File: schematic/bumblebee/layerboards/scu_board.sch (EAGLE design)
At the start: 5 parts

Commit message: RC платок аппарата
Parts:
- added P1, P2: B6B-EH-A, con-jst-eh:B6B-EH-A
- added P3: B7B-EH-A, con-jst-eh:B7B-EH-A
- added P4: B5B-EH-A, con-jst-eh:B5B-EH-A
- added P5, P6: B4B-EH-A, con-jst-eh:B4B-EH-A
- added P7: B3B-EH-A, con-jst-eh:B3B-EH-A
- added R1: (no value), ngspice-simulation:R
- added U$6: MCP2551, MCP2551:MCP2551
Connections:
- removed net LIGHT0: U$5.A0
- removed net LIGHT1: U$5.A1
- removed net LIGHT2: U$5.A2
- removed net LIGHT3: U$5.A3
- removed net LIGHT4: U$4.A0
- removed net LIGHT5: U$4.A1
- removed net LIGHT6: U$4.A2
- removed net LIGHT7: U$4.A3
- new net 5V_PCU: U$6.VDD
- new net N$10: P1.3, U$5.A2
- new net N$11: P1.2, U$5.A3
- new net N$12: P2.5, U$4.A0
- new net N$13: P2.4, U$4.A1
- new net N$14: P2.3, U$4.A2
- new net N$15: P2.2, U$4.A3
- new net N$16: U$1.PA11, U$6.RXD
- new net N$17: P3.5, U$1.PC1
- new net N$18: P3.6, U$1.PB1
- new net N$19: U$1.PA12, U$6.TXD
- new net N$20: R1.1, U$6.RS
- new net N$21: P4.2, P6.4
- new net N$22: P5.1, U$1.SW-DAT
- new net N$23: P4.3, P6.3, U$6.CANH
- new net N$24: P5.2, U$1.SW-CLK
- new net N$25: P4.4, P6.2, U$6.CANL
- new net N$26: P5.3, P7.3
- new net N$27: P5.4, P7.2
- new net N$8: P1.5, U$5.A0
- new net N$9: P1.4, U$5.A1
- net 5V_SCU: now also P1.6, P2.6, P3.7, P4.1
- net GND: now also P1.1, P2.1, P3.1, P4.5, P6.1, R1.2, U$6.VSS
- net MAG_CLOCK: now also P3.3
- net MAG_CS: now also P3.2
- net MAG_DATA: now also P3.4

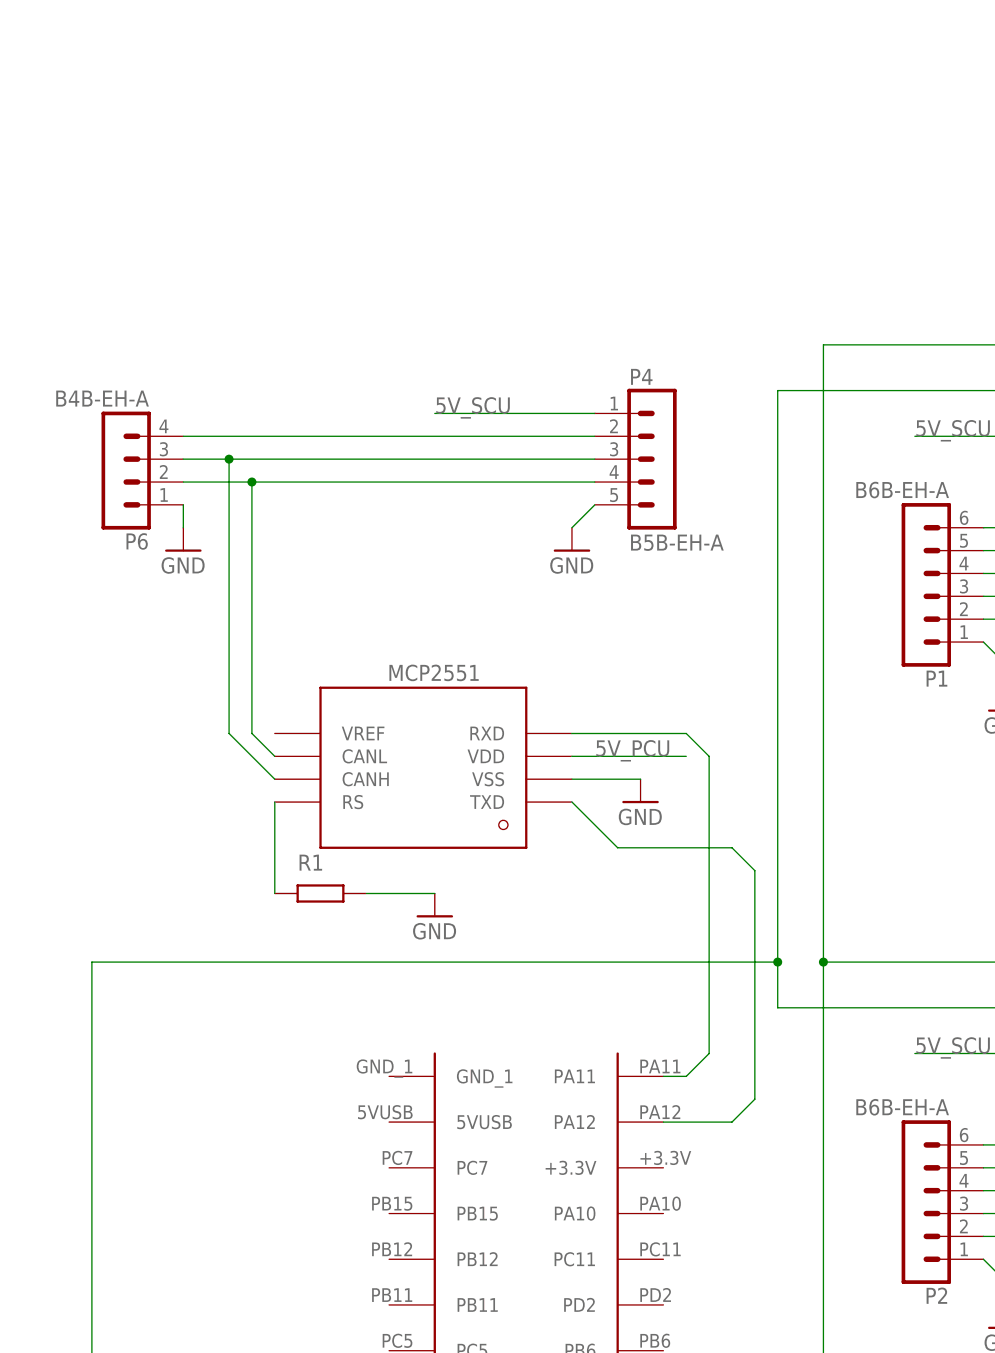
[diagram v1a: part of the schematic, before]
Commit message: Добавил либу SparkFun Идёт работа над CCU и SCU
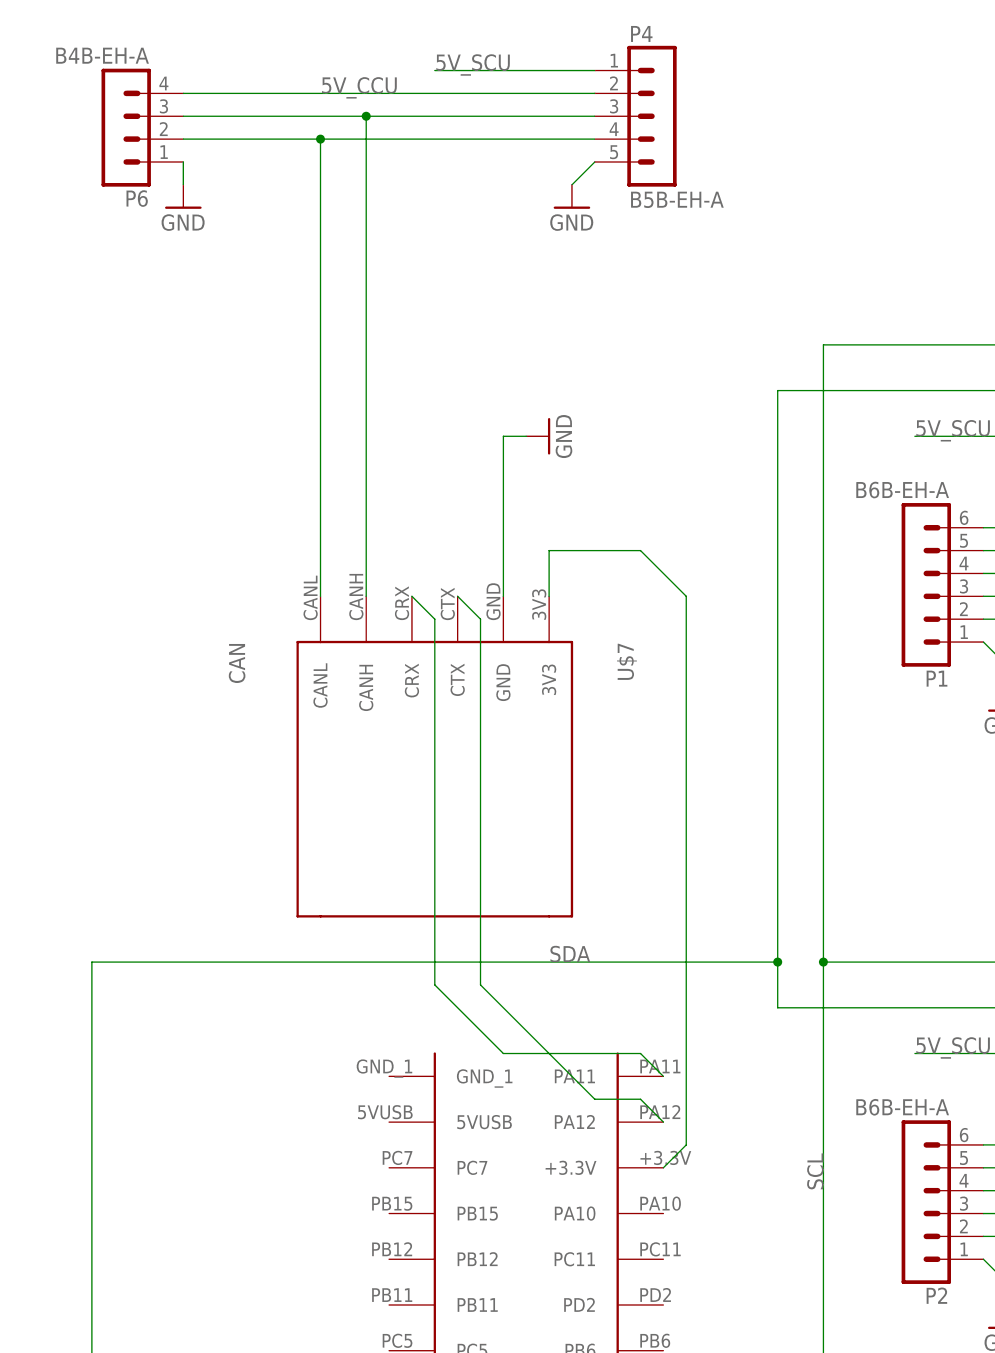
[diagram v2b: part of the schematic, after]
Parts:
- removed R1: (no value), ngspice-simulation:R
- removed U$6: MCP2551, MCP2551:MCP2551
- added U$7: CAN, bluepill:CAN
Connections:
- net N$21 renamed 5V_CCU
- net N$6 renamed SCL
- net N$7 renamed SDA
- removed net 5V_PCU: U$6.VDD
- removed net N$19: U$1.PA12, U$6.TXD
- removed net N$20: R1.1, U$6.RS
- new net N$6: U$1.PA11, U$7.CRX
- new net N$7: U$1.PA12, U$7.CTX
- net GND: now also U$7.GND; no longer R1.2, U$6.VSS
- net N$16: now also U$1.+3.3V, U$7.3V3; no longer U$1.PA11, U$6.RXD
- net N$23: now also U$7.CANH; no longer U$6.CANH
- net N$25: now also U$7.CANL; no longer U$6.CANL
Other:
- moved on the sheet: P4, P6

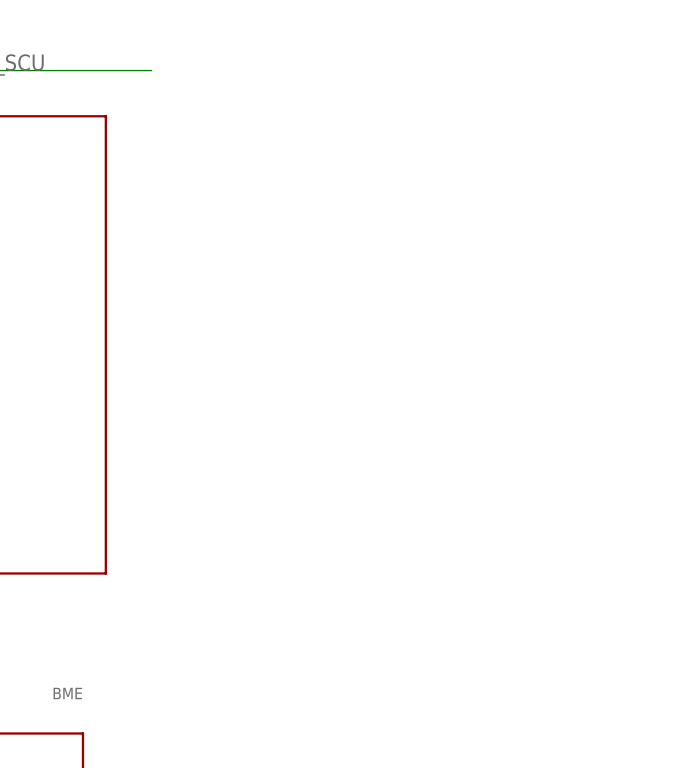
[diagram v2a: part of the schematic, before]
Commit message: Ведётся работа по платам. Готовы SCU и CCU
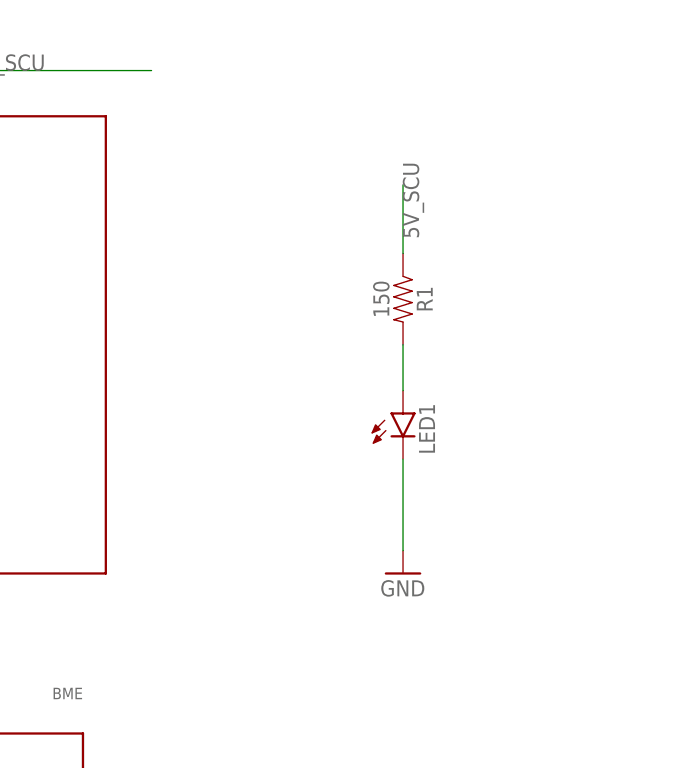
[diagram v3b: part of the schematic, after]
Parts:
- added LED1: (no value), led:LED5MM
- added R1: 150, SparkFun-Resistors:RESISTORAXIAL-0.3
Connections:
- new net N$19: LED1.A, R1.2
- net 5V_SCU: now also R1.1
- net GND: now also LED1.C

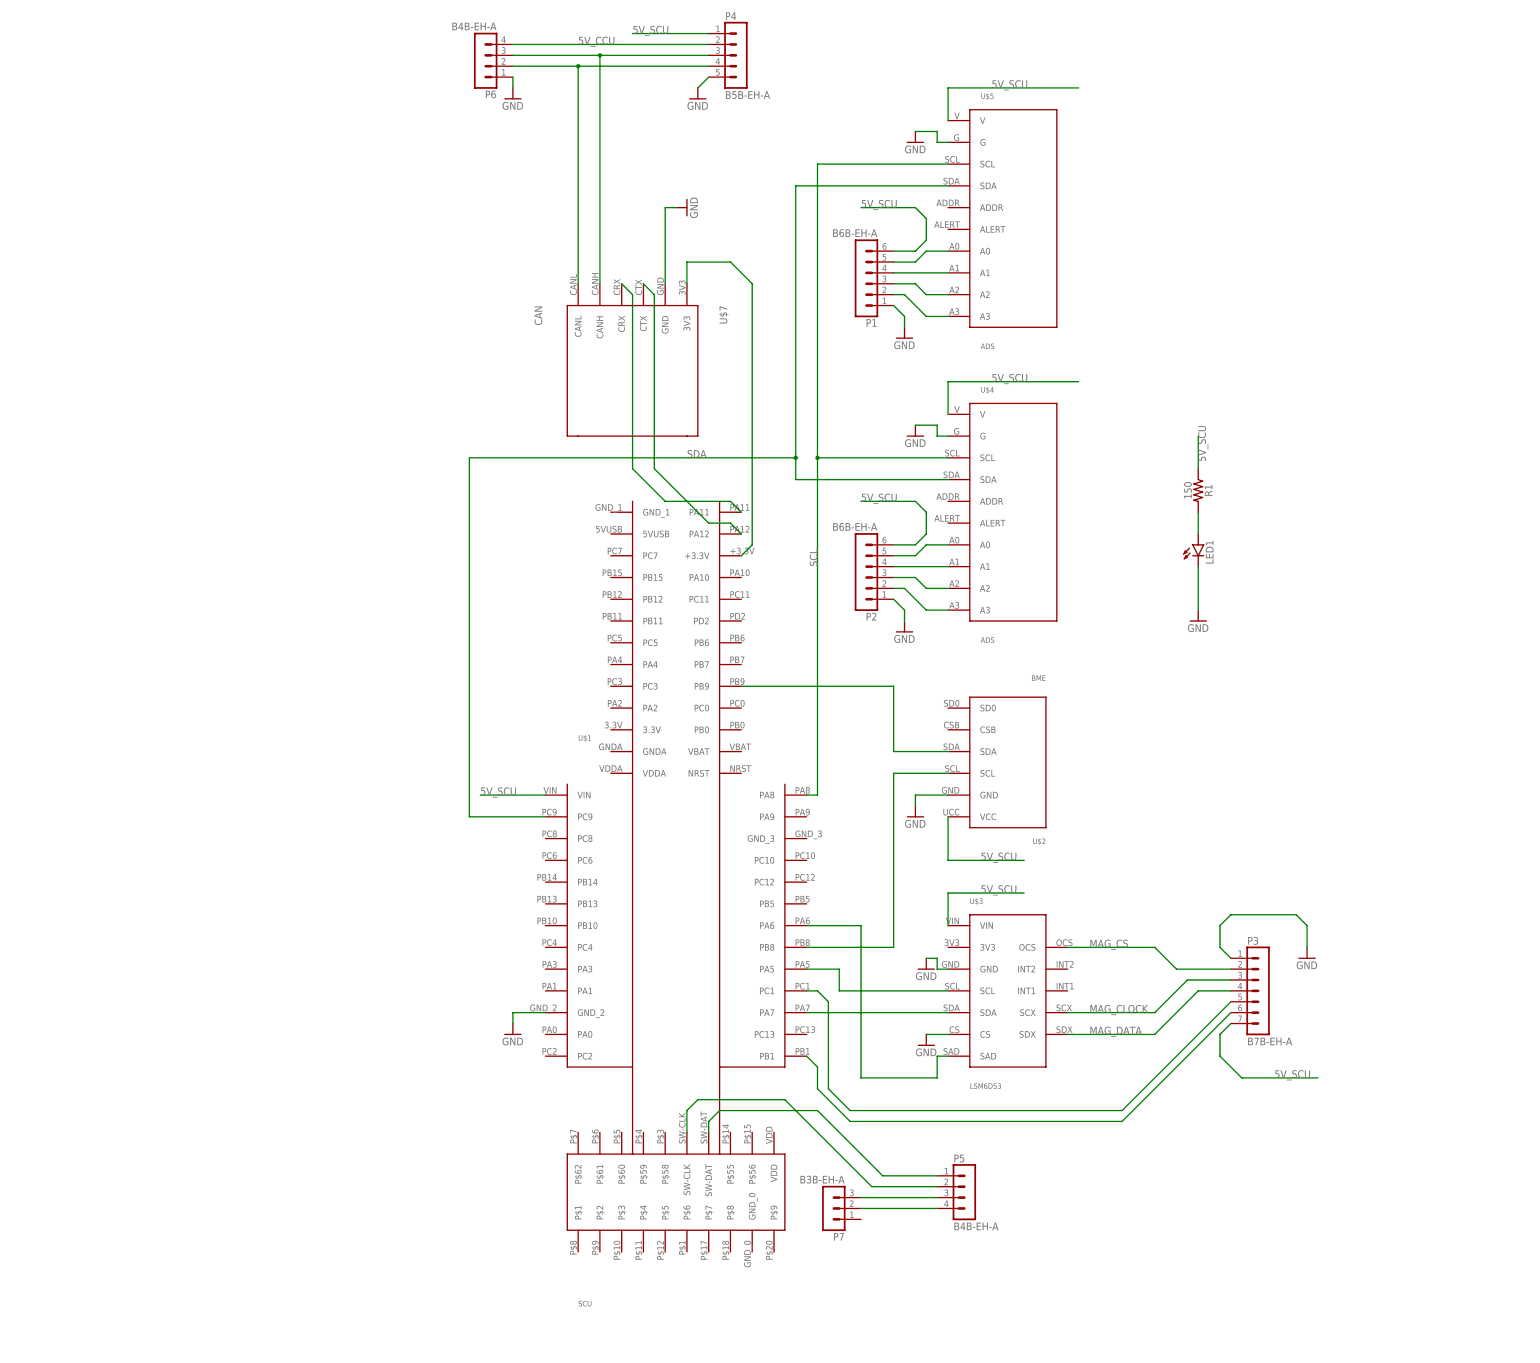
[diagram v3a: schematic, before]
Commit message: CCU и ICU полностью готовы. Было бы здорово, если бы ещё кто-то посмотрел По SCU требуются уточнения
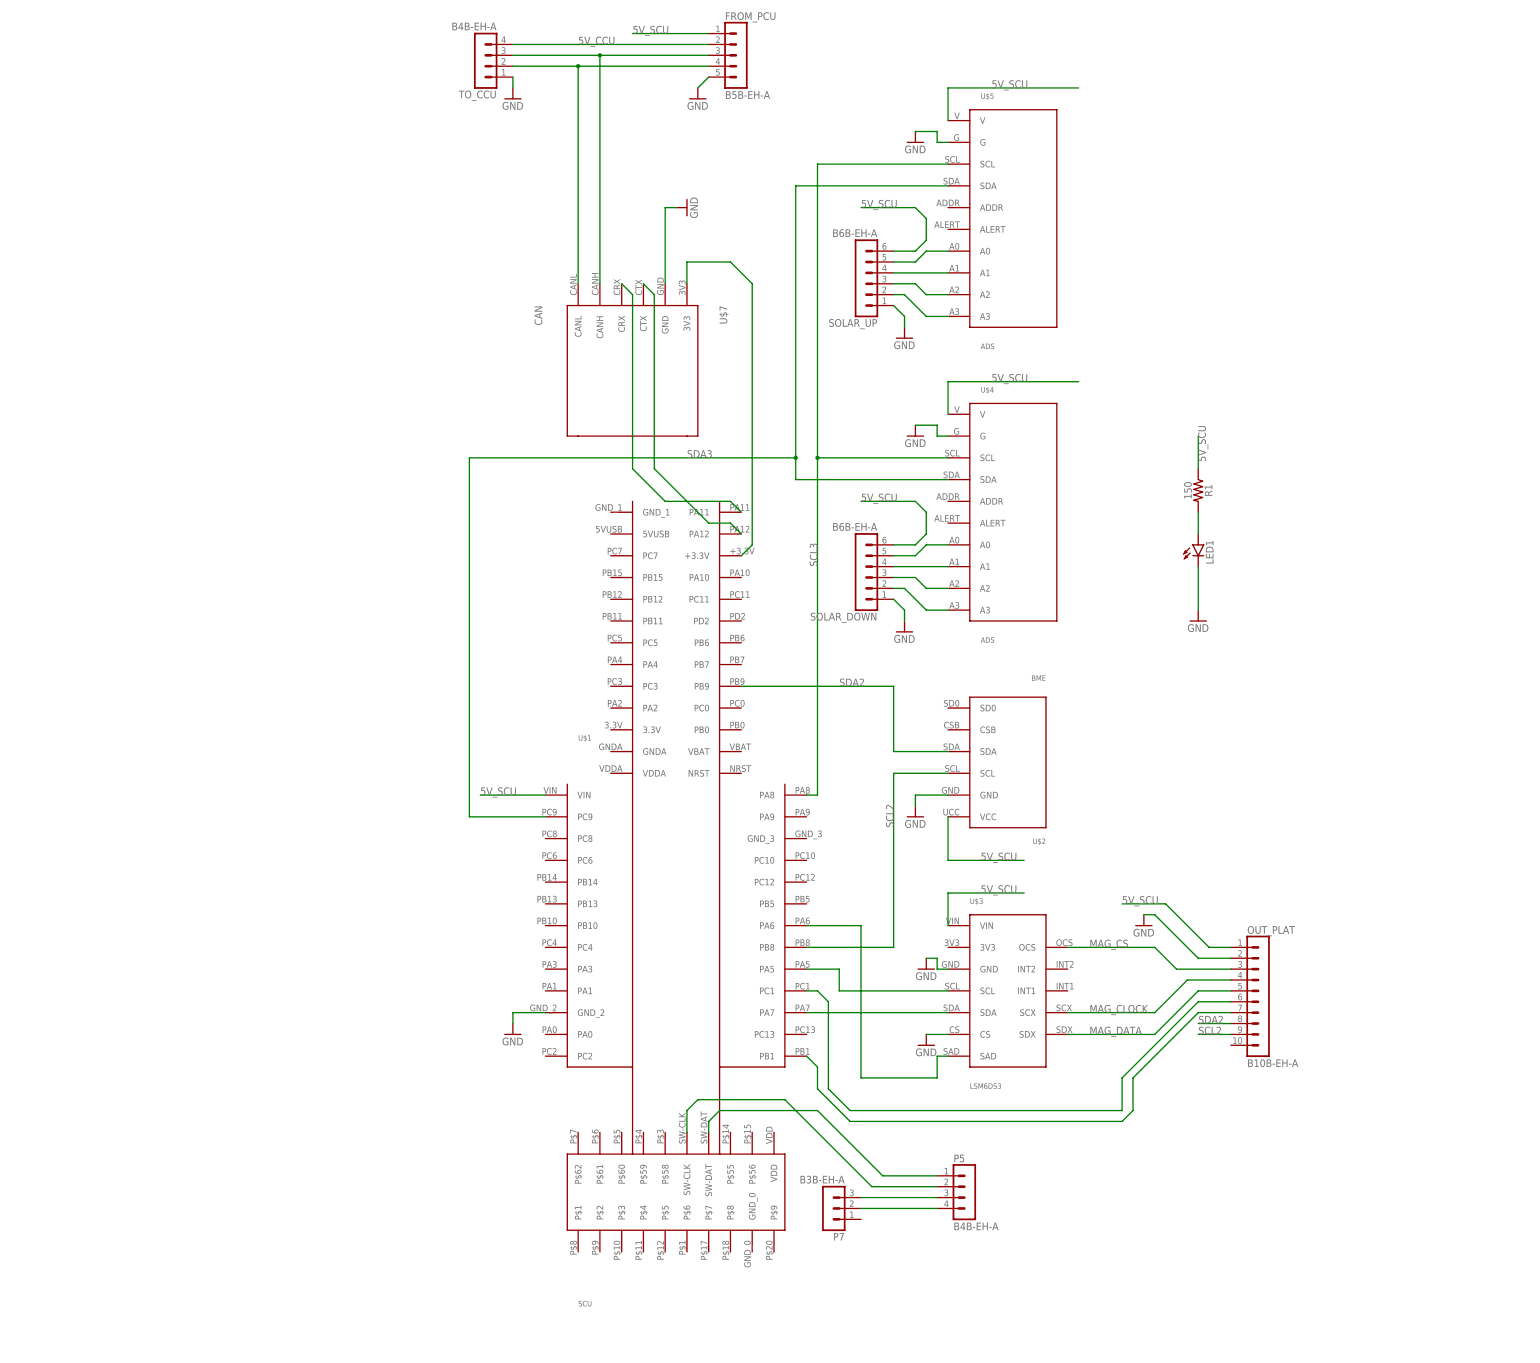
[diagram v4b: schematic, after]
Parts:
- removed P3: B7B-EH-A, con-jst-eh:B7B-EH-A
- added OUT_PLAT: B10B-EH-A, con-jst-eh:B10B-EH-A
- renumbered P1 to SOLAR_UP, P2 to SOLAR_DOWN, P4 to FROM_PCU, P6 to TO_CCU
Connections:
- net SCL renamed SCL3
- net SDA renamed SDA3
- removed net N$1: U$1.PB8, U$2.SCL
- removed net N$5: U$1.PB9, U$2.SDA
- new net SCL2: OUT_PLAT.9, U$1.PB8, U$2.SCL
- new net SDA2: OUT_PLAT.8, U$1.PB9, U$2.SDA
- net 5V_SCU: now also OUT_PLAT.1; no longer P3.7
- net GND: now also OUT_PLAT.2; no longer P3.1
- net MAG_CLOCK: now also OUT_PLAT.4; no longer P3.3
- net MAG_CS: now also OUT_PLAT.3; no longer P3.2
- net MAG_DATA: now also OUT_PLAT.5; no longer P3.4
- net N$17: now also OUT_PLAT.6; no longer P3.5
- net N$18: now also OUT_PLAT.7; no longer P3.6
